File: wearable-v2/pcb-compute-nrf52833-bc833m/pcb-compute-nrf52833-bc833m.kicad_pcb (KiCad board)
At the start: 2 copper layers, 35.1 x 19 mm, 18 parts, among them J5 HERALD_V2_CONN_PLUG, U6 BC833, U7 MX25R6435F, U8 PCF85063ATL, Y1 32.768kHz

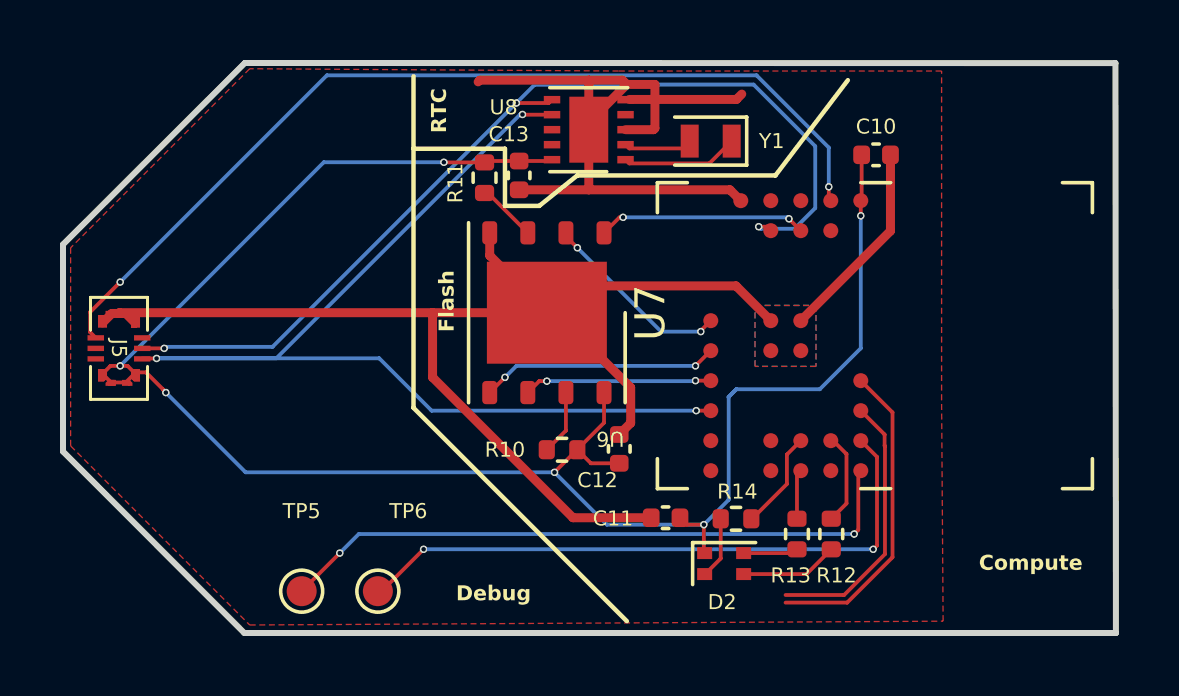
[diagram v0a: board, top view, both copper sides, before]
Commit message: Refactoring PCB files
Moved major boards into their own files.
Corrected design elements for PCBWay manufacture.
Signed-off-by: Adam Fowler <adam@adamfowler.org>
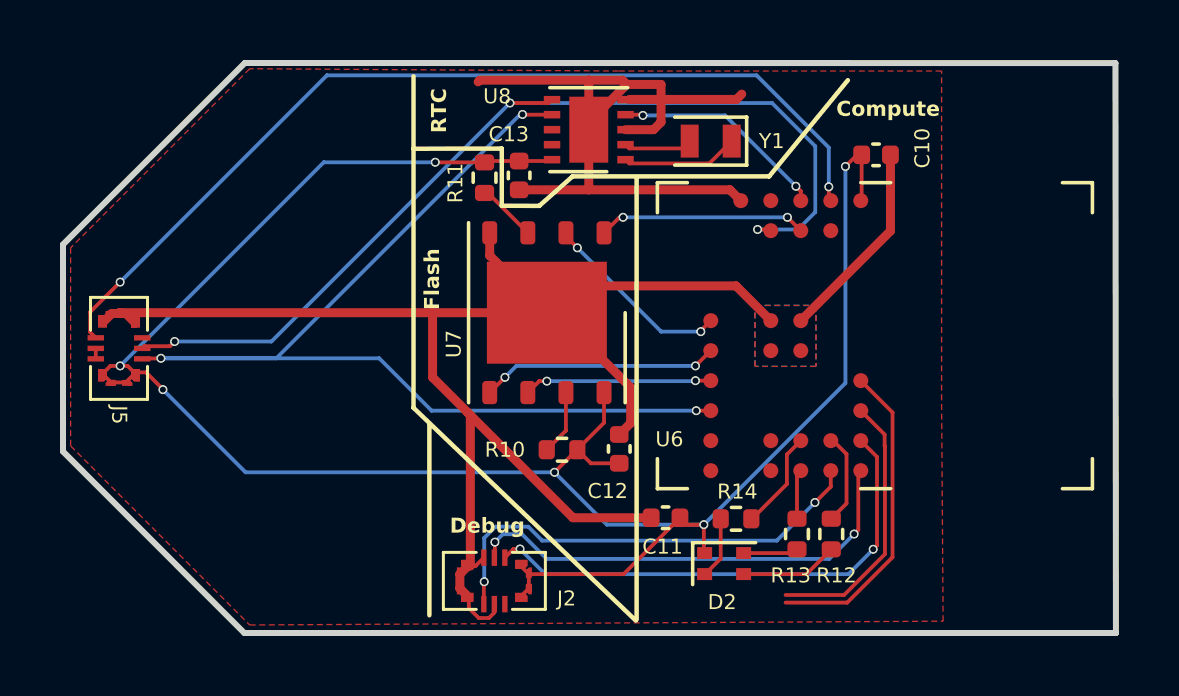
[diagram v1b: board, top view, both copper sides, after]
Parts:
- removed TP5: SWDIO, TestPoint:TestPoint_Pad_D1.0mm
- removed TP6: SWDCLK, TestPoint:TestPoint_Pad_D1.0mm
- added J2: HERALD_V2_CONN_PLUG_ARMSWD, Herald_Extras:HERALD_V2_CONN_PORT, F.Cu at (118.2, 109.1)
- J5: footprint Herald:HERALD_V2_CONN_PORT -> Herald_Extras:HERALD_V2_CONN_PORT
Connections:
- U6 pad 17: /Compute BC833M/ACC_INT1 -> /Compute BC833M/RESETn
- U6 pad 3: GND -> /Compute BC833M/RTC_INT
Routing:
- net /Compute BC833M/RESETn: track 0.00 -> 15.4 mm, vias 0 -> 2
- net GND: track 80.9 -> 89.6 mm
- net /Compute BC833M/RTC_INT: track 0.00 -> 7.21 mm, vias 0 -> 2
- net VDD: track 64.2 -> 71.0 mm
- net /Compute BC833M/SWDIO: track 21.4 -> 15.5 mm
- net /Compute BC833M/SWDCLK: track 21.0 -> 17.0 mm
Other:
- board text removed: "ConnectorStandard"

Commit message: Added accelerometer to compute module
Enable low power movement interrupt modes with just the compute module.
Signed-off-by: Adam Fowler <adam@adamfowler.org>
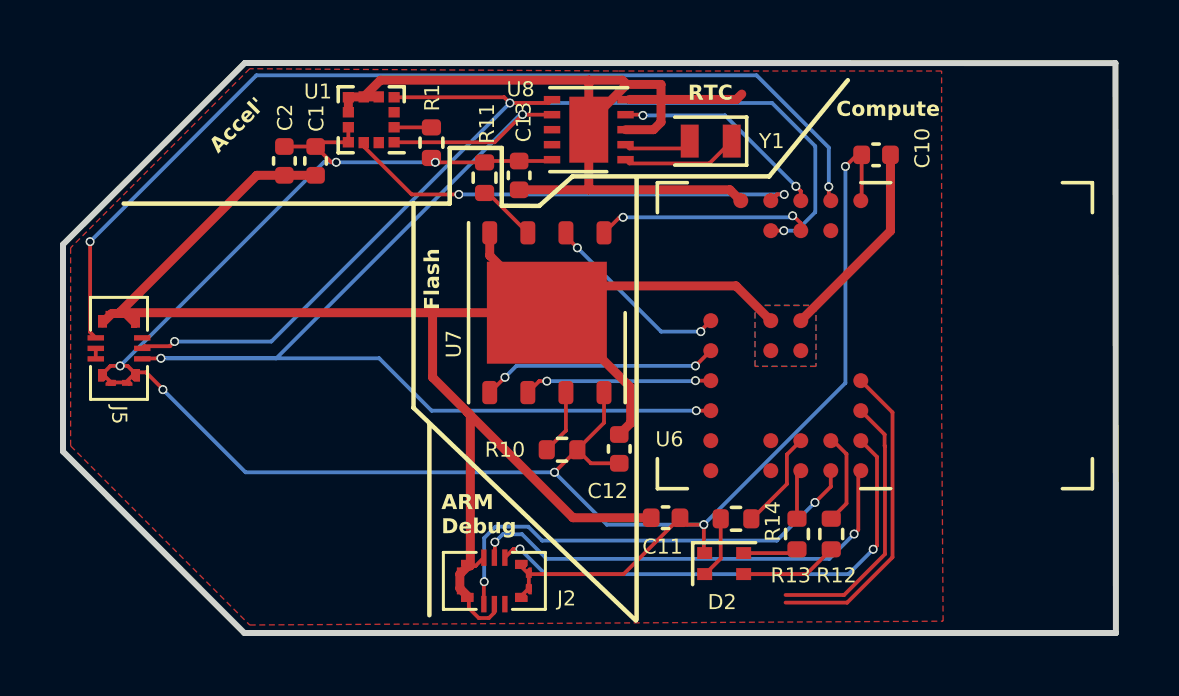
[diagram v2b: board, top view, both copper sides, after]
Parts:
- added C1: 10uF, Capacitor_SMD:C_0402_1005Metric, F.Cu at (112.3, 95.1)
- added C2: 100nF, Capacitor_SMD:C_0402_1005Metric, F.Cu at (111.2, 95.1)
- added R1: 10k, Resistor_SMD:R_0402_1005Metric, F.Cu at (116.1, 94.5)
- added U1: LIS2DE12, Package_LGA:LGA-12_2x2mm_P0.5mm, F.Cu at (114.1, 93.8)
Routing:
- net /Compute BC833M/ACC_INT2: track 0.00 -> 15.3 mm, vias 0 -> 2
- net GND: track 89.6 -> 103.6 mm
- net /Compute BC833M/SCL: track 36.4 -> 41.0 mm
- net VDD: track 71.0 -> 74.6 mm, vias 6 -> 7
- net /Compute BC833M/SDA: track 32.7 -> 35.8 mm
- net /Compute BC833M/EXT_INT1: track 31.6 -> 33.0 mm
- net Net-(U1-~{CS}): track 0.00 -> 1.25 mm
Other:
- board text added: "ARM Debug"
- board text added: "Accel'"
- board text added: "The Herald Project Compute BC833M V1.0.0 Nov 2023"
- board text removed: "Debug"

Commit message: Reworked boards for JLCPCB manufacture
Slightly larger Vias.
Added debug pin holes for Beta testing.
Signed-off-by: Adam Fowler <adam@adamfowler.org>
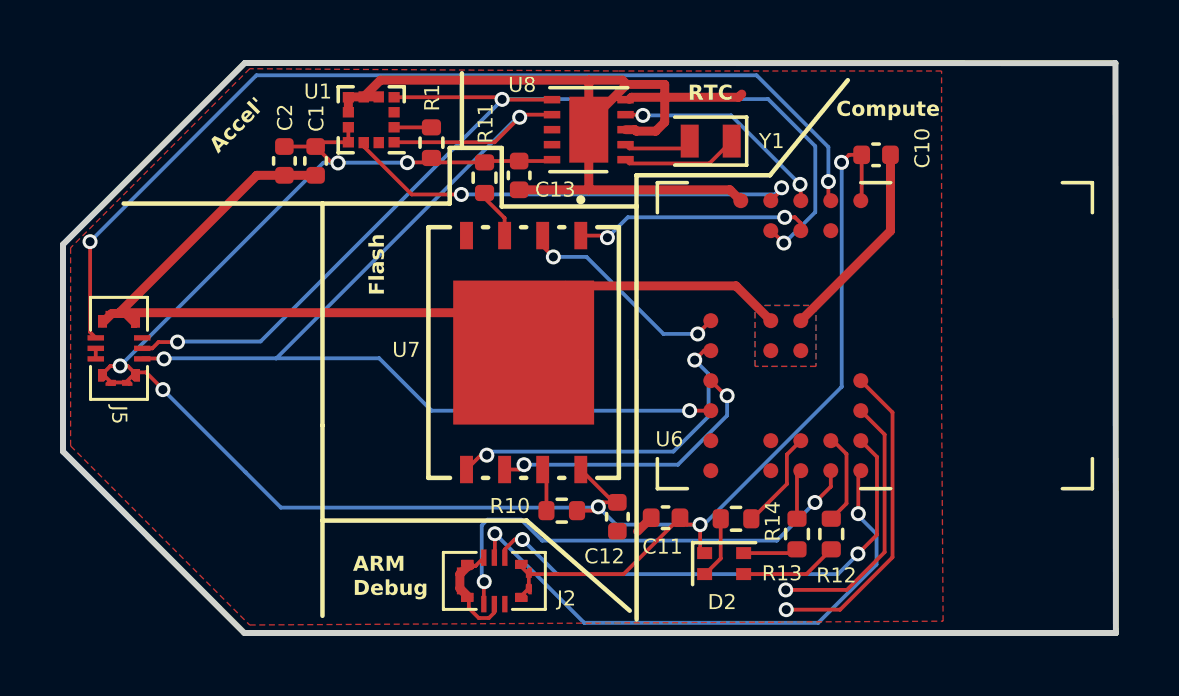
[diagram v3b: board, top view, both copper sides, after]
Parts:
- U7: footprint Package_SON:WSON-8-1EP_6x5mm_P1.27mm_EP3.4x4mm -> Herald_Extras:8-WSON_MAC
- moved C12 2.26 mm to (122.3, 107.0), turned to 90 degrees
- moved R10 2.03 mm to (120.5, 106.8)
- moved U7 1.54 mm to (119.2, 101.5)
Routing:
- net GND: track 103.6 -> 78.5 mm
- net /Compute BC833M/SCL: track 41.0 -> 36.8 mm
- net /Compute BC833M/MOSI: track 7.95 -> 11.5 mm
- net /Compute BC833M/SWDIO: track 15.5 -> 19.0 mm
- net /Compute BC833M/SCLK: track 6.34 -> 9.65 mm
- net VDD: track 74.6 -> 72.9 mm
- net /Compute BC833M/MISO: track 6.48 -> 7.41 mm
- net /Compute BC833M/FLASH_CS: track 7.15 -> 7.97 mm
- net /Compute BC833M/FLASH_RST: track 2.17 -> 1.42 mm
- net /Compute BC833M/RESETn: track 15.4 -> 15.9 mm
- net /Compute BC833M/NFC1: track 8.99 -> 8.86 mm, vias 0 -> 1
- net /Compute BC833M/NFC2: track 10.5 -> 10.6 mm, vias 0 -> 1
